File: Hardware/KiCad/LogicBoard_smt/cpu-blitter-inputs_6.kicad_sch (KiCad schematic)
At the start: 3 parts, among them IC16 7404N

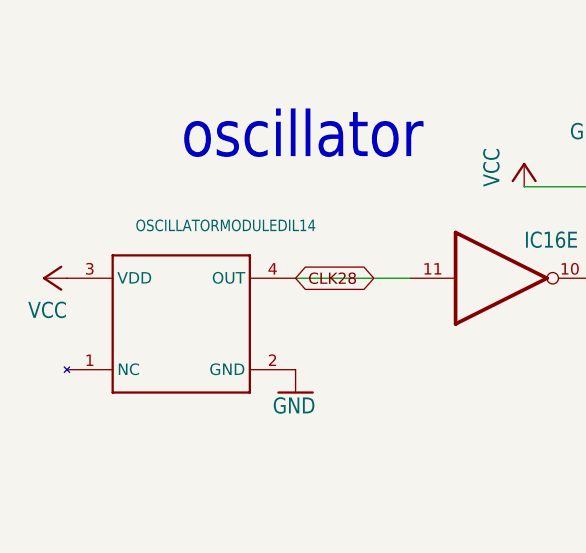
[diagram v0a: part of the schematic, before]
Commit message: updates to kicad smt versions
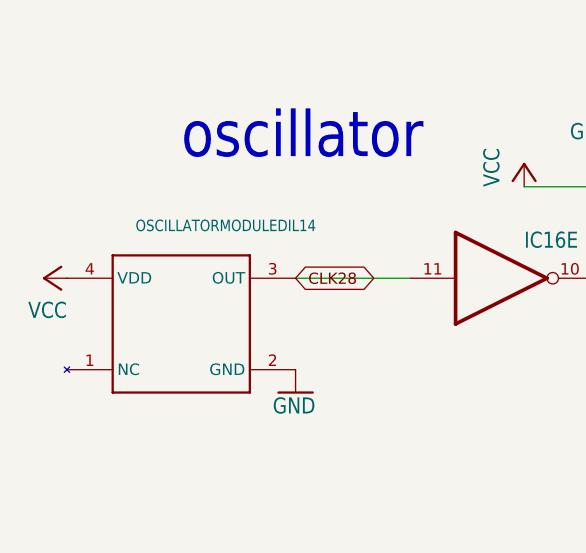
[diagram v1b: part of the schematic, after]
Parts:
- U$2: MPN LFSPXO022134Bulk -> DNI
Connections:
- net CLK28: now also U$2.3 (OUT); no longer U$2.4 (OUT)
- net VCC: now also U$2.4 (VDD); no longer U$2.3 (VDD)
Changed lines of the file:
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@@
       (effects (font (size 1.27 1.27)) hide)
     )
-    (property "MPN" "LFSPXO022134Bulk" (at 96.52 114.3 0)
+    (property "MPN" "DNI" (at 96.52 114.3 0)
       (effects (font (size 1.27 1.27)) hide)
     )

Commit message: collect production documents for quoting
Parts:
- U$2: MPN DNI -> LFSPXO022134
